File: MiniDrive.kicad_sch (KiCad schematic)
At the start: 20 parts, among them J1 Conn_LED, J2 Conn_24V, U1 TPS92200

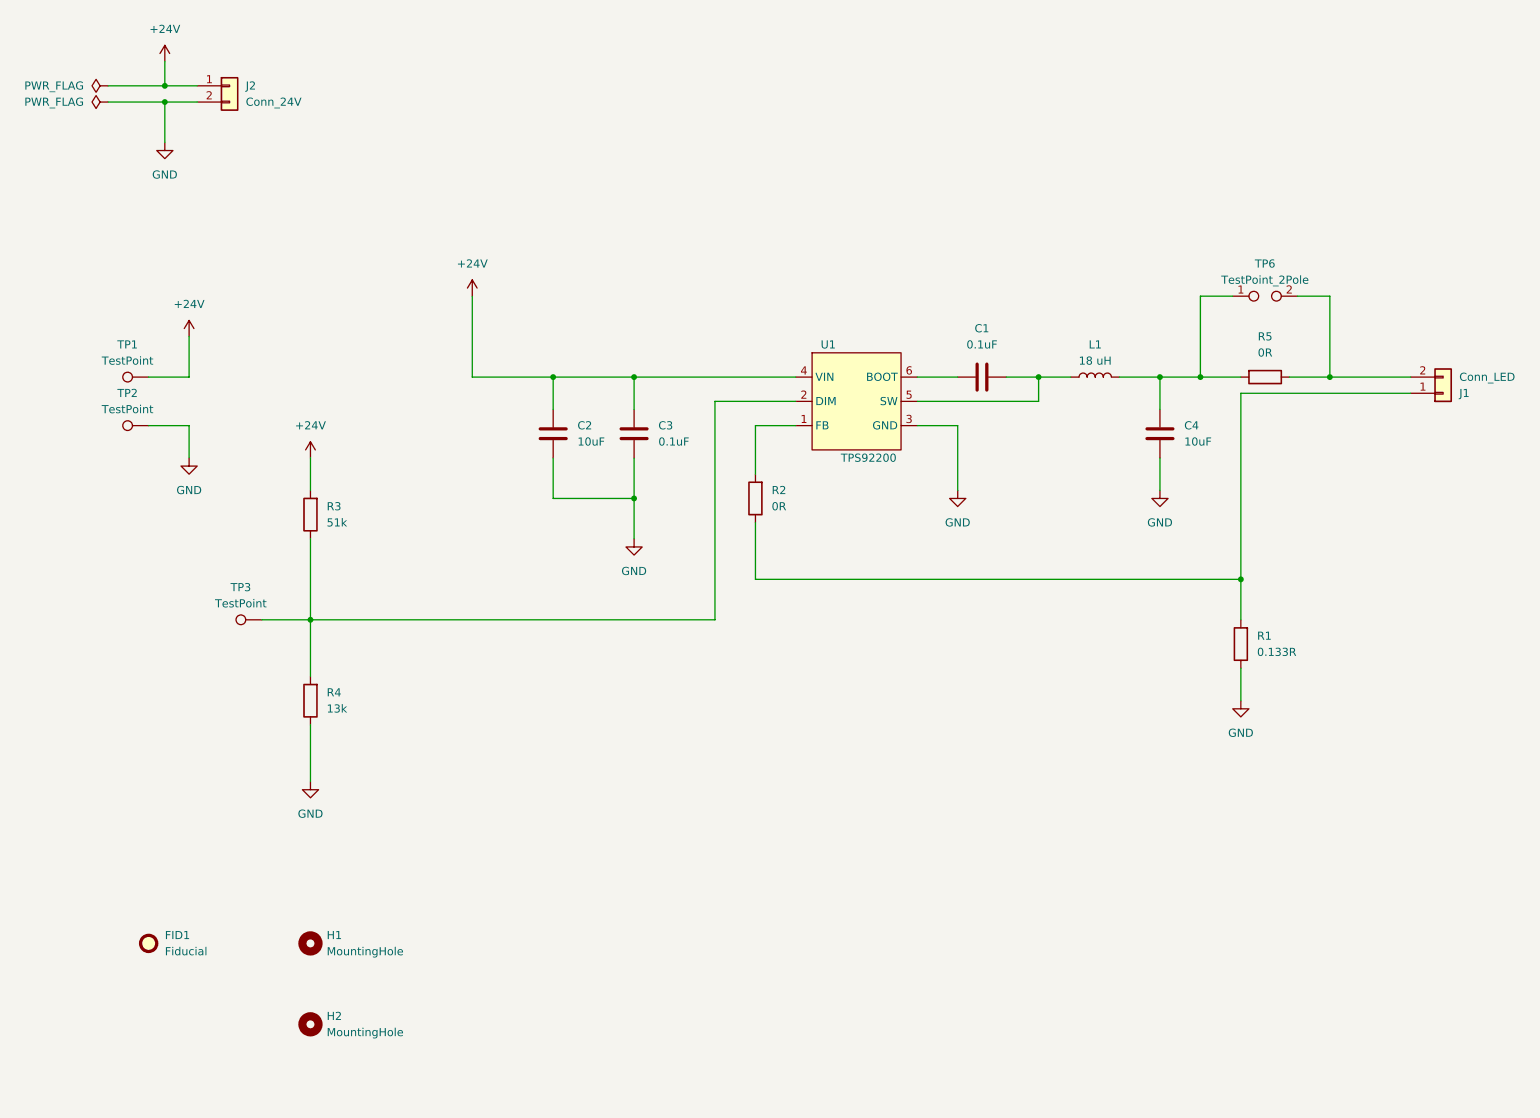
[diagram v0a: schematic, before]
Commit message: Minor layout improvements
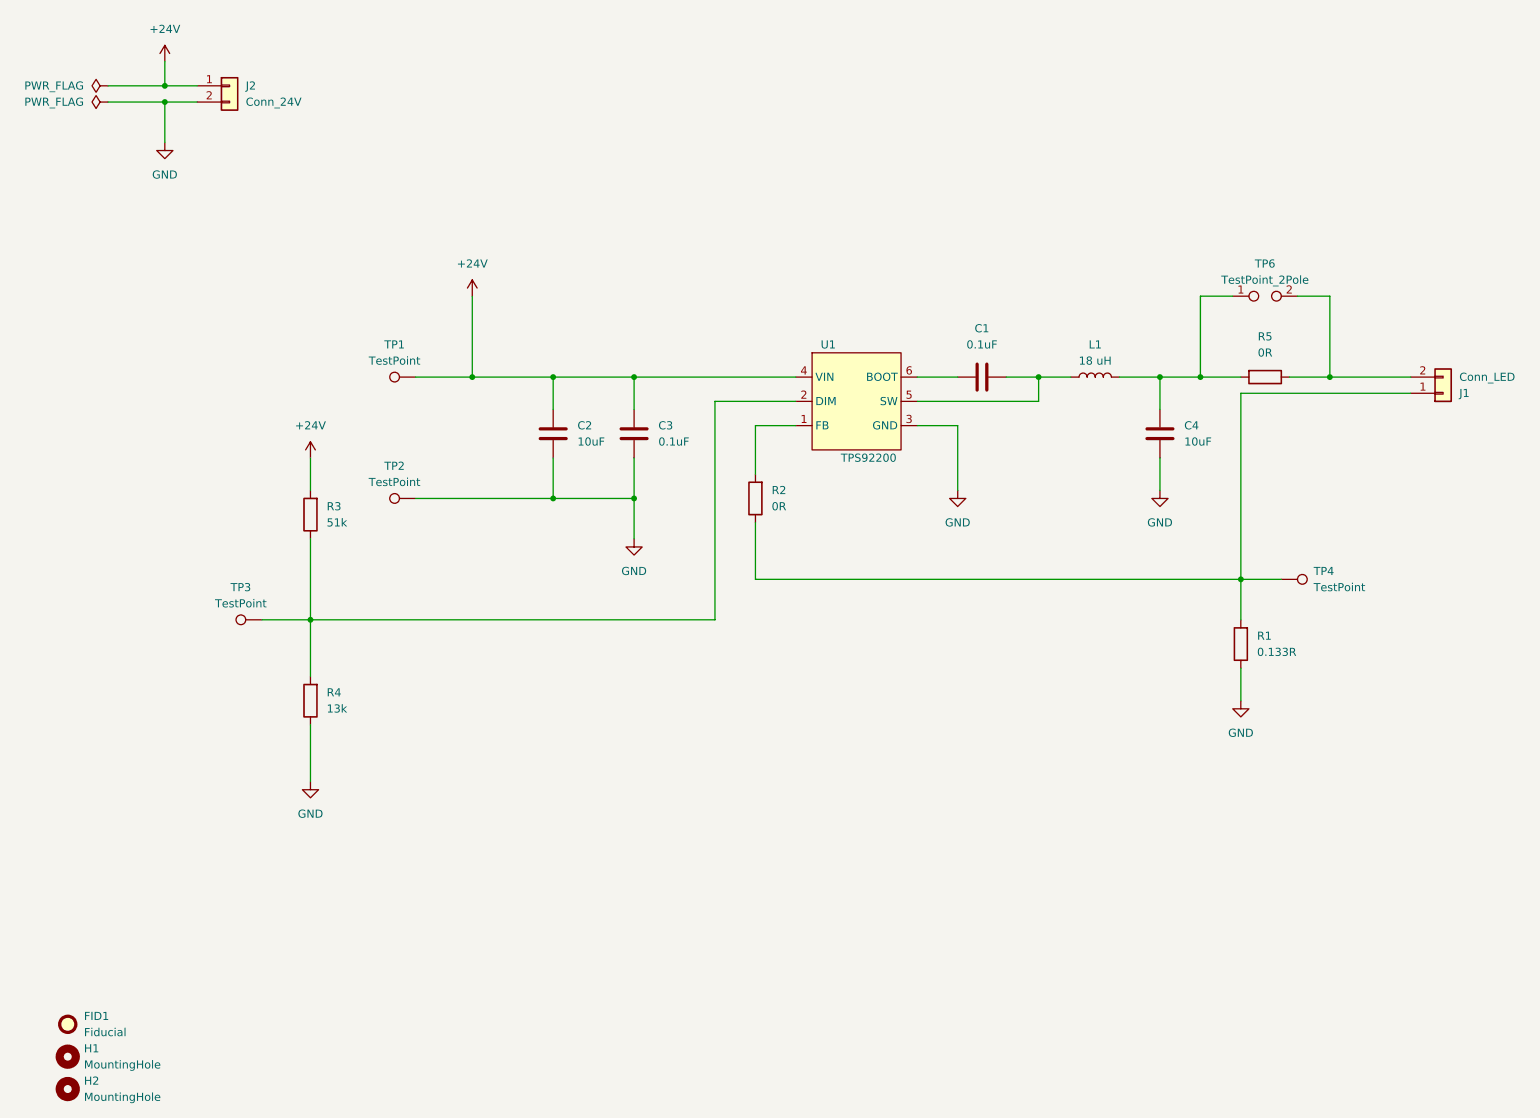
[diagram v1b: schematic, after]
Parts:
- added TP4: TestPoint, TestPoint:TestPoint_THTPad_D1.5mm_Drill0.7mm, symbol Connector:TestPoint
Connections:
- net at J1.1 (Pin_1), R1.2, R2.1: now also TP4.1
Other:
- moved on the sheet: FID1, H1, H2, TP1, TP2

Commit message: Add some in-schematic documentation as well as a DNP filter cap for FB
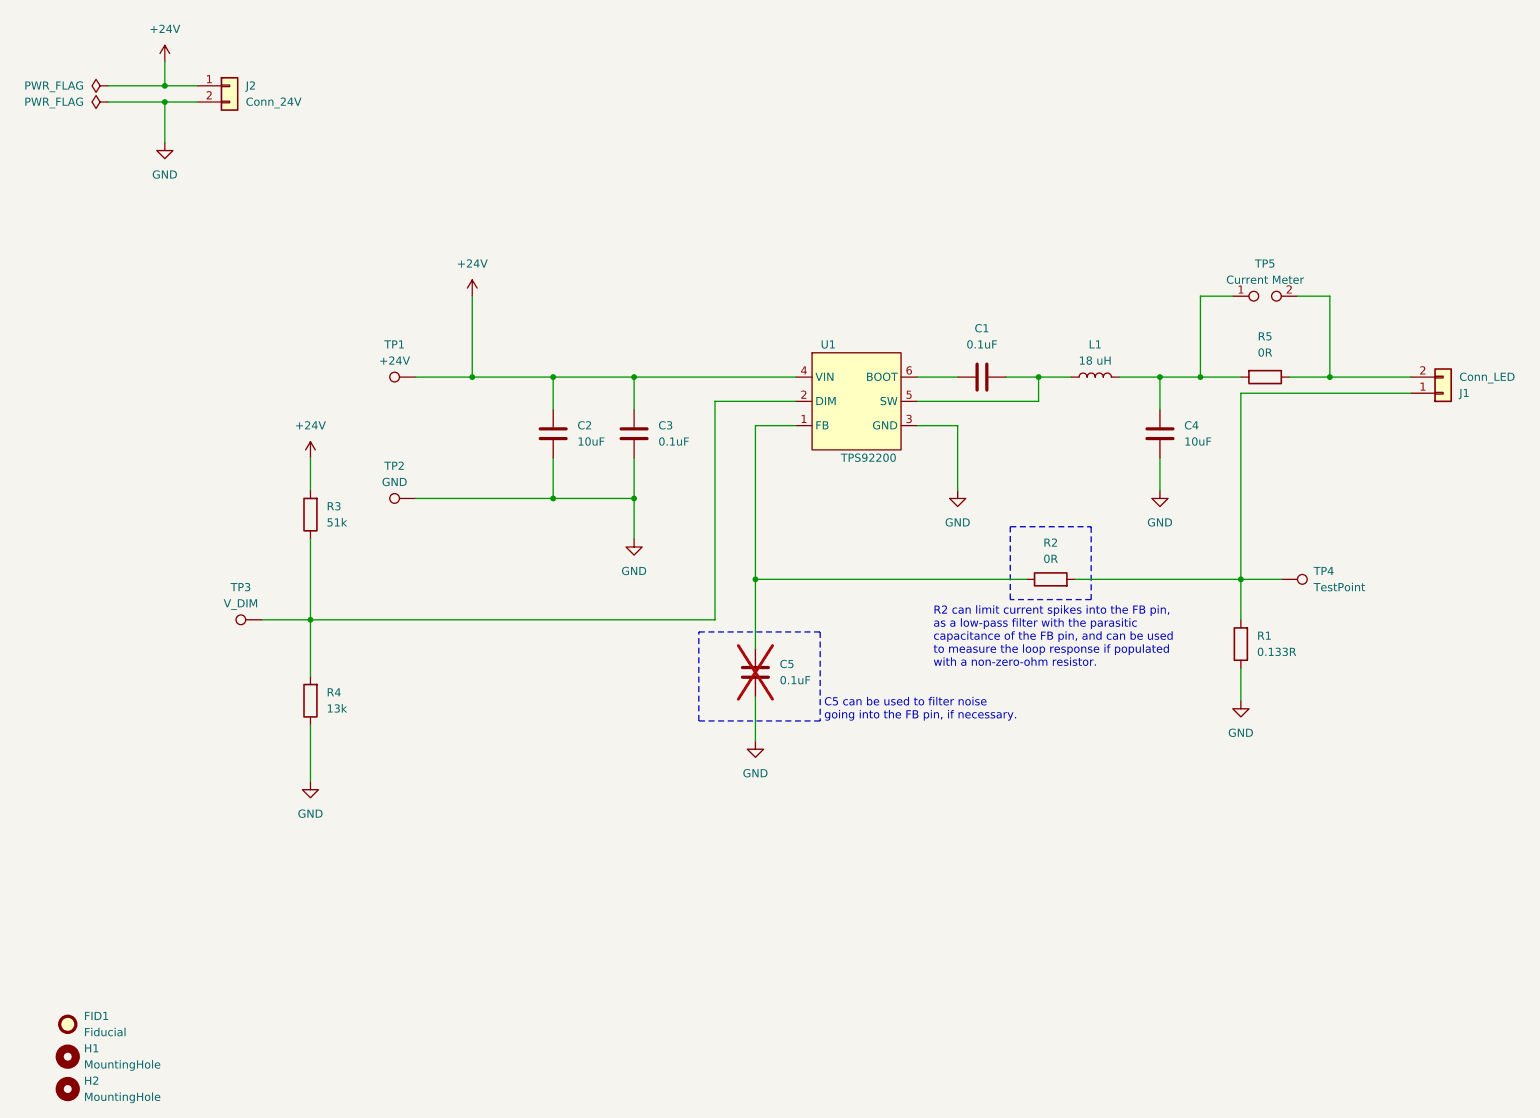
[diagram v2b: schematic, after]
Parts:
- added C5: 0.1uF, Capacitor_SMD:C_1210_3225Metric_Pad1.33x2.70mm_HandSolder, symbol Device:C
- TP1: value TestPoint -> +24V
- TP2: value TestPoint -> GND
- TP3: value TestPoint -> V_DIM
- TP5: renamed from TP6; value TestPoint_2Pole -> Current Meter
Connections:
- net GND: now also C5.2
- net at J1.1 (Pin_1), R1.2, TP4.1: now also R2.2; no longer R2.1
- net at U1.1 (FB): now also R2.1, C5.1; no longer R2.2
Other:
- note added: "C5 can be used to filter noise going into the FB pin, if necessary."
- note added: "R2 can limit current spikes into the FB pin, as a low-pass filter with the parasitic capacitance of the FB pin, and can be used to measure the loop response if populated with a non-zero-ohm resistor."
- moved on the sheet: R2
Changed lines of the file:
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@@
   (junction (at 203.2 76.2) (diameter 0) (color 0 0 0 0)
   )
+  (junction (at 133.35 107.95) (diameter 0) (color 0 0 0 0)
+  )
   (junction (at 101.6 95.25) (diameter 0) (color 0 0 0 0)
   )
@@
     (stroke (width 0) (type default))
   )
+  (wire (pts (xy 133.35 107.95) (xy 133.35 118.745))
+    (stroke (width 0) (type default))
+  )
   (wire (pts (xy 203.2 76.2) (xy 209.55 76.2))
     (stroke (width 0) (type default))
@@
     (stroke (width 0) (type default))
   )
+  (wire (pts (xy 183.515 107.95) (xy 209.55 107.95))
+    (stroke (width 0) (type default))
+  )
   (wire (pts (xy 101.6 95.25) (xy 114.3 95.25))
     (stroke (width 0) (type default))
@@
     (stroke (width 0) (type default))
   )
+  (wire (pts (xy 133.35 126.365) (xy 133.35 133.35))
+    (stroke (width 0) (type default))
+  )
   (wire (pts (xy 133.35 83.82) (xy 139.7 83.82))
     (stroke (width 0) (type default))
@@
     (stroke (width 0) (type default))
   )
-  (wire (pts (xy 133.35 83.82) (xy 133.35 91.44))
+  (wire (pts (xy 133.35 83.82) (xy 133.35 107.95))
     (stroke (width 0) (type default))
   )
@@
     (stroke (width 0) (type default))
   )
-  (wire (pts (xy 133.35 99.06) (xy 133.35 107.95))
-    (stroke (width 0) (type default))
-  )
   (wire (pts (xy 80.01 95.25) (xy 101.6 95.25))
     (stroke (width 0) (type default))
@@
     (stroke (width 0) (type default))
   )
-  (wire (pts (xy 209.55 107.95) (xy 133.35 107.95))
-    (stroke (width 0) (type default))
-  )
   (wire (pts (xy 209.55 121.92) (xy 209.55 127))
     (stroke (width 0) (type default))
   )
+  (wire (pts (xy 133.35 107.95) (xy 175.895 107.95))
+    (stroke (width 0) (type default))
+  )
   (wire (pts (xy 63.5 130.81) (xy 63.5 139.7))
     (stroke (width 0) (type default))
@@
     (stroke (width 0) (type default))
   )
+  (rectangle (start 124.46 116.205) (end 143.51 130.175)
+    (stroke (width 0) (type dash) (color 194 0 194 1))
+    (fill (type none))
+  )
+  (rectangle (start 173.355 99.695) (end 186.055 111.125)
+    (stroke (width 0) (type dash))
+    (fill (type none))
+  )
+  (text "R2 can limit current spikes into the FB pin,\nas a low-pass filter with the parasitic\ncapacitance of the FB pin, and can be used\nto measure the loop response if populated\nwith a non-zero-ohm resistor."
+    (at 161.29 121.92 0)
+    (effects (font (size 1.27 1.27)) (justify left bottom))
+  )
+  (text "C5 can be used to filter noise\ngoing into the FB pin, if necessary."
+    (at 144.145 130.175 0)
+    (effects (font (size 1.27 1.27) (color 194 0 194 1)) (justify left bottom))
+  )
+  (symbol (lib_id "power:GND") (at 133.35 133.35 0) (unit 1)
+    (in_bom yes) (on_board yes) (dnp no) (fields_autoplaced)
+    (property "Reference" "#PWR010" (at 133.35 139.7 0)
+      (effects (font (size 1.27 1.27)) hide)
+    )
+    (property "Value" "GND" (at 133.35 138.43 0)
+      (effects (font (size 1.27 1.27)))
+    )
+    (property "Footprint" "" (at 133.35 133.35 0)
+      (effects (font (size 1.27 1.27)) hide)
+    )
+    (property "Datasheet" "" (at 133.35 133.35 0)
+      (effects (font (size 1.27 1.27)) hide)
+    )
+    (pin "1")
+    (instances
+      (project "MiniDrive"
+        (path "/e06caad1-a246-4f16-9d4f-053507cbe732"
+          (reference "#PWR010") (unit 1)
+        )
+      )
+    )
+  )
   (symbol (lib_id "power:+24V") (at 88.9 63.5 0) (unit 1)
     (in_bom yes) (on_board yes) (dnp no) (fields_autoplaced)
@@
     )
   )
+  (symbol (lib_id "Device:C") (at 133.35 122.555 0) (unit 1)
+    (in_bom yes) (on_board yes) (dnp yes) (fields_autoplaced)
+    (property "Reference" "C5" (at 137.16 121.285 0)
+      (effects (font (size 1.27 1.27)) (justify left))
+    )
+    (property "Value" "0.1uF" (at 137.16 123.825 0)
+      (effects (font (size 1.27 1.27)) (justify left))
+    )
+    (property "Footprint" "Capacitor_SMD:C_1210_3225Metric_Pad1.33x2.70mm_HandSolder" (at 134.3152 126.365 0)
+      (effects (font (size 1.27 1.27)) hide)
+    )
+    (property "Datasheet" "~" (at 133.35 122.555 0)
+      (effects (font (size 1.27 1.27)) hide)
+    )
+    (pin "1")
+    (pin "2")
+    (instances
+      (project "MiniDrive"
+        (path "/e06caad1-a246-4f16-9d4f-053507cbe732"
+          (reference "C5") (unit 1)
+        )
+      )
+    )
+  )
   (symbol (lib_id "Connector:TestPoint") (at 80.01 76.2 90) (unit 1)
     (in_bom yes) (on_board yes) (dnp no) (fields_autoplaced)
@@
       (effects (font (size 1.27 1.27)))
     )
-    (property "Value" "TestPoint" (at 76.708 73.66 90)
+    (property "Value" "+24V" (at 76.708 73.66 90)
       (effects (font (size 1.27 1.27)))
     )
@@
       (effects (font (size 1.27 1.27)))
     )
-    (property "Value" "TestPoint" (at 52.578 111.76 90)
+    (property "Value" "V_DIM" (at 52.578 111.76 90)
       (effects (font (size 1.27 1.27)))
     )
@@
       (effects (font (size 1.27 1.27)))
     )
-    (property "Value" "TestPoint" (at 76.708 92.71 90)
+    (property "Value" "GND" (at 76.708 92.71 90)
       (effects (font (size 1.27 1.27)))
     )
@@
     )
   )
-  (symbol (lib_id "Device:R") (at 133.35 95.25 180) (unit 1)
-    (in_bom yes) (on_board yes) (dnp no) (fields_autoplaced)
-    (property "Reference" "R2" (at 135.89 93.98 0)
-      (effects (font (size 1.27 1.27)) (justify right))
-    )
-    (property "Value" "0R" (at 135.89 96.52 0)
-      (effects (font (size 1.27 1.27)) (justify right))
-    )
-    (property "Footprint" "Resistor_SMD:R_1206_3216Metric_Pad1.30x1.75mm_HandSolder" (at 135.128 95.25 90)
-      (effects (font (size 1.27 1.27)) hide)
-    )
-    (property "Datasheet" "~" (at 133.35 95.25 0)
+  (symbol (lib_id "Device:R") (at 179.705 107.95 90) (unit 1)
+    (in_bom yes) (on_board yes) (dnp no) (fields_autoplaced)
+    (property "Reference" "R2" (at 179.705 102.235 90)
+      (effects (font (size 1.27 1.27)))
+    )
+    (property "Value" "0R" (at 179.705 104.775 90)
+      (effects (font (size 1.27 1.27)))
+    )
+    (property "Footprint" "Resistor_SMD:R_1206_3216Metric_Pad1.30x1.75mm_HandSolder" (at 179.705 109.728 90)
+      (effects (font (size 1.27 1.27)) hide)
+    )
+    (property "Datasheet" "https://e2e.ti.com/support/power-management-group/power-management/f/power-management-forum/1217610/tps92200d2evm-about-the-value-of-rfb/4605309#4605309" (at 179.705 107.95 0)
       (effects (font (size 1.27 1.27)) hide)
     )
@@
   (symbol (lib_id "Connector:TestPoint_2Pole") (at 213.36 63.5 0) (unit 1)
     (in_bom yes) (on_board yes) (dnp no) (fields_autoplaced)
-    (property "Reference" "TP6" (at 213.36 58.42 0)
-      (effects (font (size 1.27 1.27)))
-    )
-    (property "Value" "TestPoint_2Pole" (at 213.36 60.96 0)
+    (property "Reference" "TP5" (at 213.36 58.42 0)
+      (effects (font (size 1.27 1.27)))
+    )
+    (property "Value" "Current Meter" (at 213.36 60.96 0)
       (effects (font (size 1.27 1.27)))
     )
@@
       (project "MiniDrive"
         (path "/e06caad1-a246-4f16-9d4f-053507cbe732"
-          (reference "TP6") (unit 1)
-        )
-      )
+          (reference "TP5") (unit 1)
+        )
+      )

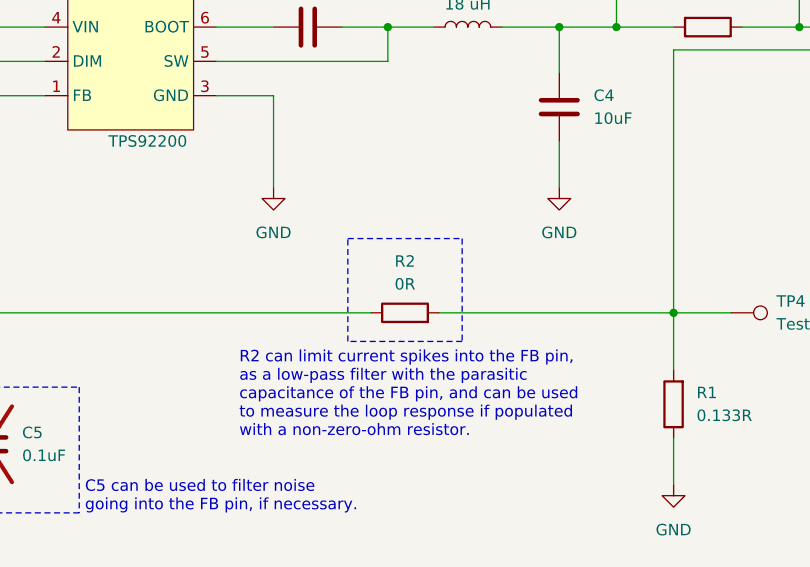
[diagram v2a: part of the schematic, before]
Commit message: Fix R2 rotation
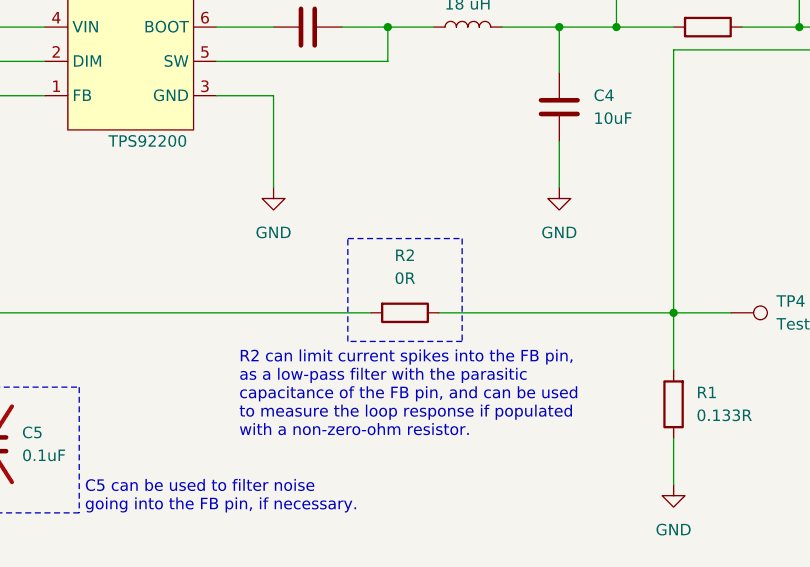
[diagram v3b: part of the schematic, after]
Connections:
- net at C5.1, U1.1 (FB): now also R2.2; no longer R2.1
- net at J1.1 (Pin_1), R1.2, TP4.1: now also R2.1; no longer R2.2
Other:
- moved on the sheet: R2
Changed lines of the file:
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@@
     )
   )
-  (symbol (lib_id "Device:R") (at 179.705 107.95 90) (unit 1)
+  (symbol (lib_id "Device:R") (at 179.705 107.95 270) (unit 1)
     (in_bom yes) (on_board yes) (dnp no) (fields_autoplaced)
-    (property "Reference" "R2" (at 179.705 102.235 90)
+    (property "Reference" "R2" (at 179.705 101.6 90)
       (effects (font (size 1.27 1.27)))
     )
-    (property "Value" "0R" (at 179.705 104.775 90)
+    (property "Value" "0R" (at 179.705 104.14 90)
       (effects (font (size 1.27 1.27)))
     )
-    (property "Footprint" "Resistor_SMD:R_1206_3216Metric_Pad1.30x1.75mm_HandSolder" (at 179.705 109.728 90)
+    (property "Footprint" "Resistor_SMD:R_1206_3216Metric_Pad1.30x1.75mm_HandSolder" (at 179.705 106.172 90)
       (effects (font (size 1.27 1.27)) hide)
     )

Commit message: Add C5 to layout
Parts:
- C5: footprint Capacitor_SMD:C_1210_3225Metric_Pad1.33x2.70mm_HandSolder -> Capacitor_SMD:C_0402_1005Metric_Pad0.74x0.62mm_HandSolder
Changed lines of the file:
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@@
       (effects (font (size 1.27 1.27)) (justify left))
     )
-    (property "Footprint" "Capacitor_SMD:C_1210_3225Metric_Pad1.33x2.70mm_HandSolder" (at 134.3152 126.365 0)
+    (property "Footprint" "Capacitor_SMD:C_0402_1005Metric_Pad0.74x0.62mm_HandSolder" (at 134.3152 126.365 0)
       (effects (font (size 1.27 1.27)) hide)
     )

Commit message: Change inductor to SMT
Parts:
- L1: footprint Inductor_THT:L_Radial_D8.7mm_P5.00mm_Fastron_07HCP -> Inductors:L_Wurth_WE-LQS-8040
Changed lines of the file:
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@@
       (effects (font (size 1.27 1.27)))
     )
-    (property "Footprint" "Inductor_THT:L_Radial_D8.7mm_P5.00mm_Fastron_07HCP" (at 186.69 76.2 0)
+    (property "Footprint" "Inductors:L_Wurth_WE-LQS-8040" (at 186.69 76.2 0)
       (effects (font (size 1.27 1.27)) hide)
     )
